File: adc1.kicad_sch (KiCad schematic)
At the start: 57 parts, among them SW1 DRV5055A4QDBZR, SW10 DRV5055A4QDBZR, SW11 DRV5055A4QDBZR, SW12 DRV5055A4QDBZR, SW13 DRV5055A4QDBZR, SW14 DRV5055A4QDBZR, SW15 DRV5055A4QDBZR, SW16 DRV5055A4QDBZR, SW2 DRV5055A4QDBZR, SW3 DRV5055A4QDBZR, SW4 DRV5055A4QDBZR, SW5 DRV5055A4QDBZR, SW6 DRV5055A4QDBZR, SW7 DRV5055A4QDBZR, SW8 DRV5055A4QDBZR, SW9 DRV5055A4QDBZR, U2 ADS7953QDBTRQ1

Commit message: rename untitle.kicad_sch to adc1.kicad_sch
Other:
- title: (none) -> MUX 1
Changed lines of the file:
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@@
 	(generator_version "10.0")
 	(paper "A4")
+	(title_block
+		(title "MUX 1")
+	)
 	(junction
 		(at 149.86 110.49)

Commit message: hierarchical module
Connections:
- net CS1 renamed ~{CS}
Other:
- title: MUX 1 -> ADC 1
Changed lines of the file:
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@@
 	(paper "A4")
 	(title_block
-		(title "MUX 1")
+		(title "ADC 1")
 	)
 	(junction
@@
 		)
 	)
-	(global_label "CS1"
+	(global_label "~{CS}"
 		(shape input)
 		(at 132.08 120.65 0)
@@
 		)
 		(property "Intersheetrefs" "${INTERSHEET_REFS}"
-			(at 138.7542 120.65 0)
+			(at 137.5447 120.65 0)
 			(hide yes)
 			(show_name no)
@@
 		)
 	)
-	(global_label "MISO"
+	(hierarchical_label "MISO"
 		(shape output)
 		(at 132.08 113.03 0)
-		(fields_autoplaced yes)
 		(effects
 			(font
@@
 			(justify left)
 		)
-		(property "Intersheetrefs" "${INTERSHEET_REFS}"
-			(at 139.6614 113.03 0)
-			(hide yes)
-			(show_name no)
-			(do_not_autoplace no)
-			(effects
-				(font
-					(size 1.27 1.27)
-				)
-				(justify left)
-			)
-		)
 	)
 	(symbol
@@
 		(instances
 			(project "stav-keeb-65"
-				(path "/f067c205-942c-45af-b694-038ca43c147c"
-					(reference "#PWR02")
-					(unit 1)
-				)
 				(path "/f067c205-942c-45af-b694-038ca43c147c/7ed9120e-f11c-4b22-935f-1ee89d31afd6"
 					(reference "#PWR02")
@@
 		(instances
 			(project "stav-keeb-65"
-				(path "/f067c205-942c-45af-b694-038ca43c147c"
-					(reference "U2")
-					(unit 1)
-				)
 				(path "/f067c205-942c-45af-b694-038ca43c147c/7ed9120e-f11c-4b22-935f-1ee89d31afd6"
 					(reference "U2")
@@
 		(instances
 			(project "stav-keeb-65"
-				(path "/f067c205-942c-45af-b694-038ca43c147c"
-					(reference "R1")
-					(unit 1)
-				)
 				(path "/f067c205-942c-45af-b694-038ca43c147c/7ed9120e-f11c-4b22-935f-1ee89d31afd6"
 					(reference "R1")
@@
 		(instances
 			(project "stav-keeb-65"
-				(path "/f067c205-942c-45af-b694-038ca43c147c"
-					(reference "SW1")
-					(unit 1)
-				)
 				(path "/f067c205-942c-45af-b694-038ca43c147c/7ed9120e-f11c-4b22-935f-1ee89d31afd6"
 					(reference "SW1")
@@
 		(instances
 			(project "stav-keeb-65"
-				(path "/f067c205-942c-45af-b694-038ca43c147c"
-					(reference "C1")
-					(unit 1)
-				)
 				(path "/f067c205-942c-45af-b694-038ca43c147c/7ed9120e-f11c-4b22-935f-1ee89d31afd6"
 					(reference "C1")

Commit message: Power & USB
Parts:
- C1, C10, C11, C12, C13, C14, C15, C16, C17, C2, C20, C21, C3, C4, C5, C6, C7, C8, C9: footprint Capacitor_SMD:C_0201_0603Metric_Pad0.64x0.40mm_HandSolder -> Capacitor_SMD:C_0603_1608Metric_Pad1.08x0.95mm_HandSolder
- R1, R10, R11, R12, R13, R14, R15, R16, R2, R3, R4, R5, R6, R7, R8, R9: footprint Resistor_SMD:R_0201_0603Metric_Pad0.64x0.40mm_HandSolder -> Resistor_SMD:R_0603_1608Metric_Pad0.98x0.95mm_HandSolder
- R17, R18, R19, R20: footprint Resistor_SMD:R_0201_0603Metric_Pad0.64x0.40mm_HandSolder -> Capacitor_SMD:C_0603_1608Metric_Pad1.08x0.95mm_HandSolder
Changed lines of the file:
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@@
 			)
 		)
-		(property "Footprint" "Capacitor_SMD:C_0201_0603Metric_Pad0.64x0.40mm_HandSolder"
+		(property "Footprint" "Capacitor_SMD:C_0603_1608Metric_Pad1.08x0.95mm_HandSolder"
 			(at 232.41 66.3448 0)
 			(hide yes)
@@
 			)
 		)
-		(property "Footprint" "Resistor_SMD:R_0201_0603Metric_Pad0.64x0.40mm_HandSolder"
+		(property "Footprint" "Resistor_SMD:R_0603_1608Metric_Pad0.98x0.95mm_HandSolder"
 			(at 98.806 131.826 90)
 			(hide yes)
@@
 			)
 		)
-		(property "Footprint" "Capacitor_SMD:C_0201_0603Metric_Pad0.64x0.40mm_HandSolder"
+		(property "Footprint" "Capacitor_SMD:C_0603_1608Metric_Pad1.08x0.95mm_HandSolder"
 			(at 95.25 35.8648 0)
 			(hide yes)
@@
 			)
 		)
-		(property "Footprint" "Capacitor_SMD:C_0201_0603Metric_Pad0.64x0.40mm_HandSolder"
+		(property "Footprint" "Capacitor_SMD:C_0603_1608Metric_Pad1.08x0.95mm_HandSolder"
 			(at 60.96 66.3448 0)
 			(hide yes)
@@
 			)
 		)
-		(property "Footprint" "Capacitor_SMD:C_0201_0603Metric_Pad0.64x0.40mm_HandSolder"
+		(property "Footprint" "Capacitor_SMD:C_0603_1608Metric_Pad1.08x0.95mm_HandSolder"
 			(at 198.12 66.3448 0)
 			(hide yes)
@@
 			)
 		)
-		(property "Footprint" "Capacitor_SMD:C_0201_0603Metric_Pad0.64x0.40mm_HandSolder"
+		(property "Footprint" "Capacitor_SMD:C_0603_1608Metric_Pad1.08x0.95mm_HandSolder"
 			(at 153.3652 125.73 0)
 			(hide yes)
@@
 			)
 		)
-		(property "Footprint" "Resistor_SMD:R_0201_0603Metric_Pad0.64x0.40mm_HandSolder"
+		(property "Footprint" "Resistor_SMD:R_0603_1608Metric_Pad0.98x0.95mm_HandSolder"
 			(at 151.384 134.874 90)
 			(hide yes)
@@
 			)
 		)
-		(property "Footprint" "Capacitor_SMD:C_0201_0603Metric_Pad0.64x0.40mm_HandSolder"
+		(property "Footprint" "Capacitor_SMD:C_0603_1608Metric_Pad1.08x0.95mm_HandSolder"
 			(at 163.83 35.8648 0)
 			(hide yes)
@@
 			)
 		)
-		(property "Footprint" "Resistor_SMD:R_0201_0603Metric_Pad0.64x0.40mm_HandSolder"
+		(property "Footprint" "Capacitor_SMD:C_0603_1608Metric_Pad1.08x0.95mm_HandSolder"
 			(at 132.334 97.536 90)
 			(hide yes)
@@
 			)
 		)
-		(property "Footprint" "Capacitor_SMD:C_0201_0603Metric_Pad0.64x0.40mm_HandSolder"
+		(property "Footprint" "Capacitor_SMD:C_0603_1608Metric_Pad1.08x0.95mm_HandSolder"
 			(at 163.83 66.3448 0)
 			(hide yes)
@@
 			)
 		)
-		(property "Footprint" "Resistor_SMD:R_0201_0603Metric_Pad0.64x0.40mm_HandSolder"
+		(property "Footprint" "Resistor_SMD:R_0603_1608Metric_Pad0.98x0.95mm_HandSolder"
 			(at 151.384 129.794 90)
 			(hide yes)
@@
 			)
 		)
-		(property "Footprint" "Capacitor_SMD:C_0201_0603Metric_Pad0.64x0.40mm_HandSolder"
+		(property "Footprint" "Capacitor_SMD:C_0603_1608Metric_Pad1.08x0.95mm_HandSolder"
 			(at 232.41 35.8648 0)
 			(hide yes)
@@
 			)
 		)
-		(property "Footprint" "Capacitor_SMD:C_0201_0603Metric_Pad0.64x0.40mm_HandSolder"
+		(property "Footprint" "Capacitor_SMD:C_0603_1608Metric_Pad1.08x0.95mm_HandSolder"
 			(at 86.0552 120.65 0)
 			(hide yes)
@@
 			)
 		)
-		(property "Footprint" "Capacitor_SMD:C_0201_0603Metric_Pad0.64x0.40mm_HandSolder"
+		(property "Footprint" "Capacitor_SMD:C_0603_1608Metric_Pad1.08x0.95mm_HandSolder"
 			(at 60.96 35.8648 0)
 			(hide yes)
@@
 			)
 		)
-		(property "Footprint" "Capacitor_SMD:C_0201_0603Metric_Pad0.64x0.40mm_HandSolder"
+		(property "Footprint" "Capacitor_SMD:C_0603_1608Metric_Pad1.08x0.95mm_HandSolder"
 			(at 129.54 35.8648 0)
 			(hide yes)
@@
 			)
 		)
-		(property "Footprint" "Capacitor_SMD:C_0201_0603Metric_Pad0.64x0.40mm_HandSolder"
+		(property "Footprint" "Capacitor_SMD:C_0603_1608Metric_Pad1.08x0.95mm_HandSolder"
 			(at 95.25 66.3448 0)
 			(hide yes)
@@
 			)
 		)
-		(property "Footprint" "Capacitor_SMD:C_0201_0603Metric_Pad0.64x0.40mm_HandSolder"
+		(property "Footprint" "Capacitor_SMD:C_0603_1608Metric_Pad1.08x0.95mm_HandSolder"
 			(at 129.54 66.3447 0)
 			(hide yes)
@@
 			)
 		)
-		(property "Footprint" "Resistor_SMD:R_0201_0603Metric_Pad0.64x0.40mm_HandSolder"
+		(property "Footprint" "Resistor_SMD:R_0603_1608Metric_Pad0.98x0.95mm_HandSolder"
 			(at 134.874 127.254 90)
 			(hide yes)
@@
 			)
 		)
-		(property "Footprint" "Resistor_SMD:R_0201_0603Metric_Pad0.64x0.40mm_HandSolder"
+		(property "Footprint" "Capacitor_SMD:C_0603_1608Metric_Pad1.08x0.95mm_HandSolder"
 			(at 101.854 97.536 90)
 			(hide yes)
@@
 			)
 		)
-		(property "Footprint" "Resistor_SMD:R_0201_0603Metric_Pad0.64x0.40mm_HandSolder"
+		(property "Footprint" "Capacitor_SMD:C_0603_1608Metric_Pad1.08x0.95mm_HandSolder"
 			(at 138.684 97.536 90)
 			(hide yes)
@@
 			)
 		)
-		(property "Footprint" "Capacitor_SMD:C_0201_0603Metric_Pad0.64x0.40mm_HandSolder"
+		(property "Footprint" "Capacitor_SMD:C_0603_1608Metric_Pad1.08x0.95mm_HandSolder"
 			(at 26.67 66.3448 0)
 			(hide yes)
@@
 			)
 		)
-		(property "Footprint" "Capacitor_SMD:C_0201_0603Metric_Pad0.64x0.40mm_HandSolder"
+		(property "Footprint" "Capacitor_SMD:C_0603_1608Metric_Pad1.08x0.95mm_HandSolder"
 			(at 150.8252 110.49 0)
 			(hide yes)
@@
 			)
 		)
-		(property "Footprint" "Resistor_SMD:R_0201_0603Metric_Pad0.64x0.40mm_HandSolder"
+		(property "Footprint" "Resistor_SMD:R_0603_1608Metric_Pad0.98x0.95mm_HandSolder"
 			(at 134.874 132.334 90)
 			(hide yes)
@@
 			)
 		)
-		(property "Footprint" "Resistor_SMD:R_0201_0603Metric_Pad0.64x0.40mm_HandSolder"
+		(property "Footprint" "Resistor_SMD:R_0603_1608Metric_Pad0.98x0.95mm_HandSolder"
 			(at 98.806 136.906 90)
 			(hide yes)
@@
 			)
 		)
-		(property "Footprint" "Resistor_SMD:R_0201_0603Metric_Pad0.64x0.40mm_HandSolder"
+		(property "Footprint" "Capacitor_SMD:C_0603_1608Metric_Pad1.08x0.95mm_HandSolder"
 			(at 95.504 97.536 90)
 			(hide yes)
@@
 			)
 		)
-		(property "Footprint" "Capacitor_SMD:C_0201_0603Metric_Pad0.64x0.40mm_HandSolder"
+		(property "Footprint" "Capacitor_SMD:C_0603_1608Metric_Pad1.08x0.95mm_HandSolder"
 			(at 198.12 35.8648 0)
 			(hide yes)
@@
 			)
 		)
-		(property "Footprint" "Resistor_SMD:R_0201_0603Metric_Pad0.64x0.40mm_HandSolder"
+		(property "Footprint" "Resistor_SMD:R_0603_1608Metric_Pad0.98x0.95mm_HandSolder"
 			(at 98.806 147.066 90)
 			(hide yes)
@@
 			)
 		)
-		(property "Footprint" "Resistor_SMD:R_0201_0603Metric_Pad0.64x0.40mm_HandSolder"
+		(property "Footprint" "Resistor_SMD:R_0603_1608Metric_Pad0.98x0.95mm_HandSolder"
 			(at 81.026 144.526 90)
 			(hide yes)
@@
 			)
 		)
-		(property "Footprint" "Resistor_SMD:R_0201_0603Metric_Pad0.64x0.40mm_HandSolder"
+		(property "Footprint" "Resistor_SMD:R_0603_1608Metric_Pad0.98x0.95mm_HandSolder"
 			(at 81.026 139.446 90)
 			(hide yes)
@@
 			)
 		)
-		(property "Footprint" "Capacitor_SMD:C_0201_0603Metric_Pad0.64x0.40mm_HandSolder"
+		(property "Footprint" "Capacitor_SMD:C_0603_1608Metric_Pad1.08x0.95mm_HandSolder"
 			(at 266.7 35.8647 0)
 			(hide yes)
@@
 			)
 		)
-		(property "Footprint" "Resistor_SMD:R_0201_0603Metric_Pad0.64x0.40mm_HandSolder"
+		(property "Footprint" "Resistor_SMD:R_0603_1608Metric_Pad0.98x0.95mm_HandSolder"
 			(at 81.026 129.286 90)
 			(hide yes)
@@
 			)
 		)
-		(property "Footprint" "Resistor_SMD:R_0201_0603Metric_Pad0.64x0.40mm_HandSolder"
+		(property "Footprint" "Resistor_SMD:R_0603_1608Metric_Pad0.98x0.95mm_HandSolder"
 			(at 134.874 137.414 90)
 			(hide yes)
@@
 			)
 		)
-		(property "Footprint" "Capacitor_SMD:C_0201_0603Metric_Pad0.64x0.40mm_HandSolder"
+		(property "Footprint" "Capacitor_SMD:C_0603_1608Metric_Pad1.08x0.95mm_HandSolder"
 			(at 27.94 35.8648 0)
 			(hide yes)
@@
 			)
 		)
-		(property "Footprint" "Resistor_SMD:R_0201_0603Metric_Pad0.64x0.40mm_HandSolder"
+		(property "Footprint" "Resistor_SMD:R_0603_1608Metric_Pad0.98x0.95mm_HandSolder"
 			(at 151.384 139.954 90)
 			(hide yes)
@@
 			)
 		)
-		(property "Footprint" "Resistor_SMD:R_0201_0603Metric_Pad0.64x0.40mm_HandSolder"
+		(property "Footprint" "Resistor_SMD:R_0603_1608Metric_Pad0.98x0.95mm_HandSolder"
 			(at 81.026 134.366 90)
 			(hide yes)
@@
 			)
 		)
-		(property "Footprint" "Resistor_SMD:R_0201_0603Metric_Pad0.64x0.40mm_HandSolder"
+		(property "Footprint" "Resistor_SMD:R_0603_1608Metric_Pad0.98x0.95mm_HandSolder"
 			(at 134.874 142.494 90)
 			(hide yes)
@@
 			)
 		)
-		(property "Footprint" "Resistor_SMD:R_0201_0603Metric_Pad0.64x0.40mm_HandSolder"
+		(property "Footprint" "Resistor_SMD:R_0603_1608Metric_Pad0.98x0.95mm_HandSolder"
 			(at 98.806 141.986 90)
 			(hide yes)
@@
 			)
 		)
-		(property "Footprint" "Resistor_SMD:R_0201_0603Metric_Pad0.64x0.40mm_HandSolder"
+		(property "Footprint" "Resistor_SMD:R_0603_1608Metric_Pad0.98x0.95mm_HandSolder"
 			(at 151.384 145.034 90)
 			(hide yes)
@@
 			)
 		)
-		(property "Footprint" "Capacitor_SMD:C_0201_0603Metric_Pad0.64x0.40mm_HandSolder"
+		(property "Footprint" "Capacitor_SMD:C_0603_1608Metric_Pad1.08x0.95mm_HandSolder"
 			(at 266.7 66.3447 0)
 			(hide yes)

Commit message: 2.5V ref
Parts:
- added C130: 1uF, Capacitor_SMD:C_0603_1608Metric_Pad1.08x0.95mm_HandSolder, symbol Device:C
- C19: value 10uF -> 100nF; footprint Capacitor_SMD:C_0805_2012Metric_Pad1.18x1.45mm_HandSolder -> Capacitor_SMD:C_0603_1608Metric_Pad1.08x0.95mm_HandSolder; LCSC Part C15850 -> C14663
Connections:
- net GND: now also C19.2, C130.1; no longer C19.1
- net +2V5 renamed +2V5_RREF
- net +2V5_RREF: now also C19.1, C130.2; no longer C19.2

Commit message: Change 2.5V ref to voltage divider
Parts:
- R17, R18, R19, R20: footprint Capacitor_SMD:C_0603_1608Metric_Pad1.08x0.95mm_HandSolder -> Resistor_SMD:R_0603_1608Metric_Pad0.98x0.95mm_HandSolder
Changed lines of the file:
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@@
 			)
 		)
-		(property "Footprint" "Capacitor_SMD:C_0603_1608Metric_Pad1.08x0.95mm_HandSolder"
+		(property "Footprint" "Resistor_SMD:R_0603_1608Metric_Pad0.98x0.95mm_HandSolder"
 			(at 132.334 97.536 90)
 			(hide yes)
@@
 			)
 		)
-		(property "Footprint" "Capacitor_SMD:C_0603_1608Metric_Pad1.08x0.95mm_HandSolder"
+		(property "Footprint" "Resistor_SMD:R_0603_1608Metric_Pad0.98x0.95mm_HandSolder"
 			(at 101.854 97.536 90)
 			(hide yes)
@@
 			)
 		)
-		(property "Footprint" "Capacitor_SMD:C_0603_1608Metric_Pad1.08x0.95mm_HandSolder"
+		(property "Footprint" "Resistor_SMD:R_0603_1608Metric_Pad0.98x0.95mm_HandSolder"
 			(at 138.684 97.536 90)
 			(hide yes)
@@
 			)
 		)
-		(property "Footprint" "Capacitor_SMD:C_0603_1608Metric_Pad1.08x0.95mm_HandSolder"
+		(property "Footprint" "Resistor_SMD:R_0603_1608Metric_Pad0.98x0.95mm_HandSolder"
 			(at 95.504 97.536 90)
 			(hide yes)

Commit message: Review fixes
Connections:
- net +2V5_RREF renamed +2V5_REF

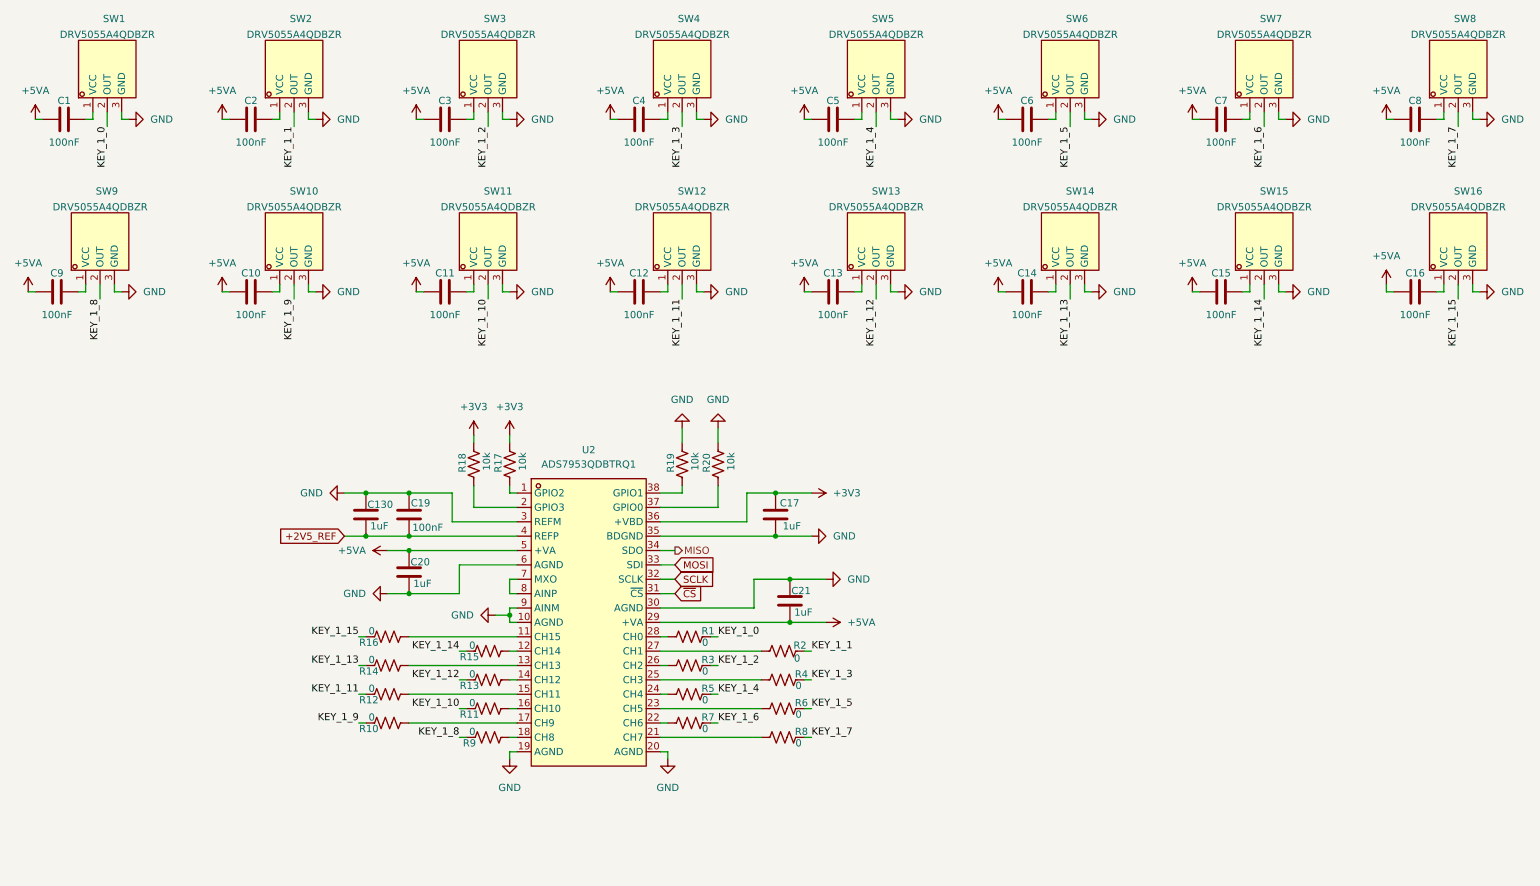
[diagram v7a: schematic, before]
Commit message: initial script for sensor placement, and schematic fixes
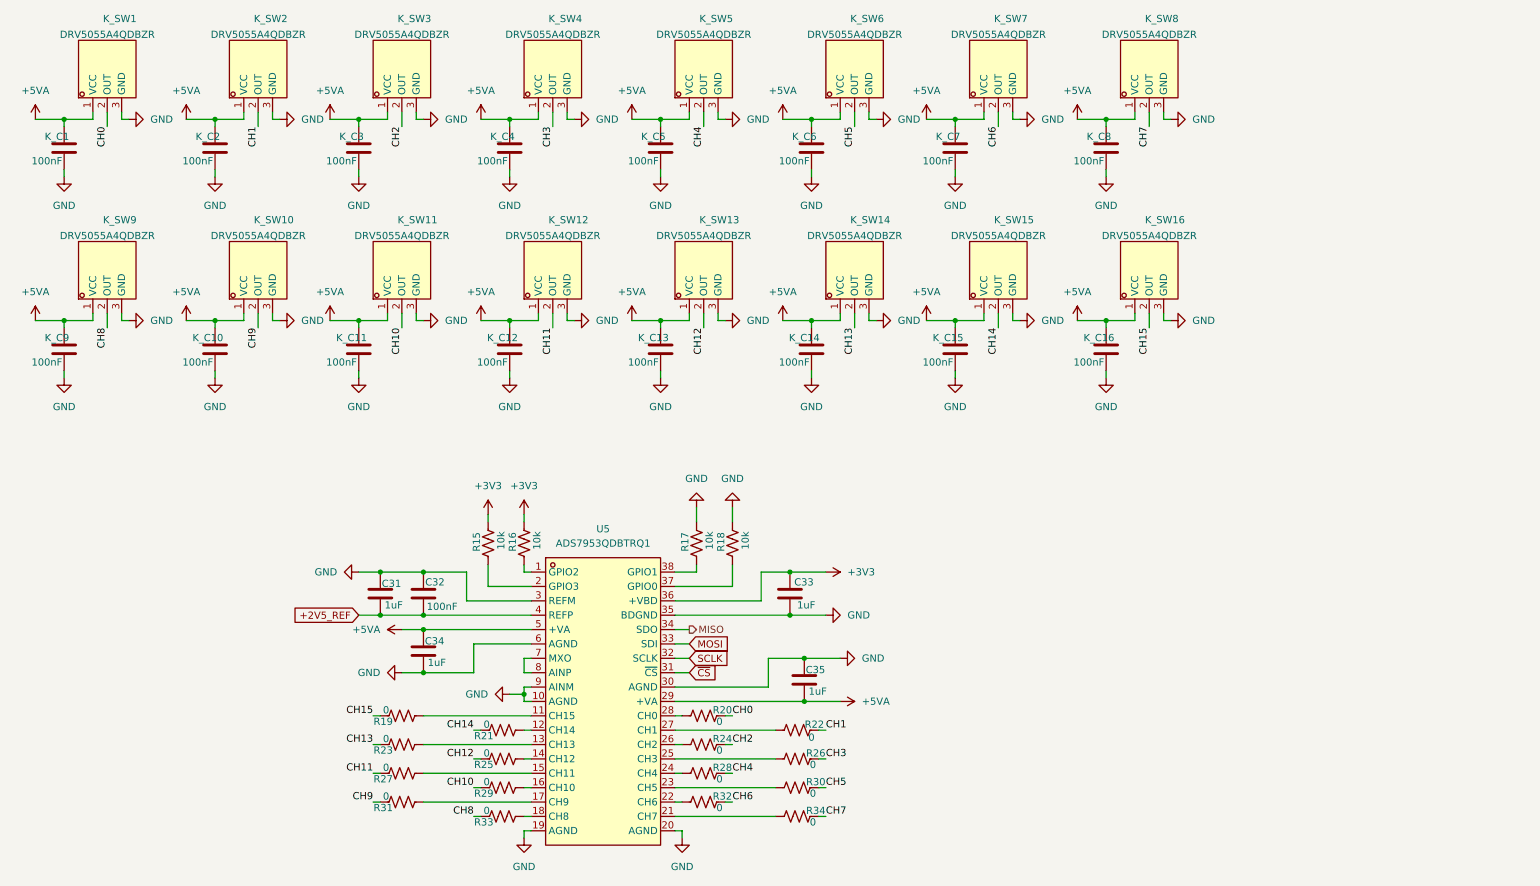
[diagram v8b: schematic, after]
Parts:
- removed C1, C10, C11, C12, C13, C14, C15, C16, C2, C3, C4, C5, C6, C7, C8, C9: 100nF, Capacitor_SMD:C_0603_1608Metric_Pad1.08x0.95mm_HandSolder, symbol Device:C
- removed SW10, SW11, SW12, SW13, SW14, SW15, SW16, SW2, SW3, SW4, SW5, SW6, SW7, SW8, SW9: DRV5055A4QDBZR, easyeda2kicad:SOT-23-3_L2.9-W1.3-P1.90-LS2.4-BR, symbol easyeda2kicad:DRV5055A4QDBZR
- added K_C1, K_C10, K_C11, K_C12, K_C13, K_C14, K_C15, K_C16, K_C2, K_C3, K_C4, K_C5, K_C6, K_C7, K_C8, K_C9: 100nF, Capacitor_SMD:C_0603_1608Metric_Pad1.08x0.95mm_HandSolder, symbol Device:C
- added K_SW10, K_SW11, K_SW12, K_SW13, K_SW14, K_SW15, K_SW16, K_SW2, K_SW3, K_SW4, K_SW5, K_SW6, K_SW7, K_SW8, K_SW9: DRV5055A4QDBZR, easyeda2kicad:SOT-23-3_L2.9-W1.3-P1.90-LS2.4-BR, symbol easyeda2kicad:DRV5055A4QDBZR
- renumbered C130 to C31, C19 to C32, C17 to C33, C20 to C34, C21 to C35, SW1 to K_SW1, R18 to R15, R17 to R16, R19 to R17, R20 to R18, R16 to R19, R1 to R20, R15 to R21, R2 to R22, R14 to R23, R3 to R24, R13 to R25, R4 to R26, R12 to R27, R5 to R28, R11 to R29, R6 to R30, R10 to R31, R7 to R32, R9 to R33, R8 to R34, U2 to U5
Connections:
- net +5VA: now also K_SW1.1 (VCC), K_C1.2, K_C10.2, K_C11.2, K_C12.2, K_C13.2, K_C14.2, K_C15.2, K_C16.2, K_C2.2, K_C3.2, K_C4.2, K_C5.2, K_C6.2, K_C7.2, K_C8.2, K_C9.2, K_SW10.1 (VCC), K_SW11.1 (VCC), K_SW12.1 (VCC), K_SW13.1 (VCC), K_SW14.1 (VCC), K_SW15.1 (VCC), K_SW16.1 (VCC), K_SW2.1 (VCC), K_SW3.1 (VCC), K_SW4.1 (VCC), K_SW5.1 (VCC), K_SW6.1 (VCC), K_SW7.1 (VCC), K_SW8.1 (VCC), K_SW9.1 (VCC)
- net GND: now also K_C1.1, K_C10.1, K_C11.1, K_C12.1, K_C13.1, K_C14.1, K_C15.1, K_C16.1, K_C2.1, K_C3.1, K_C4.1, K_C5.1, K_C6.1, K_C7.1, K_C8.1, K_C9.1, K_SW10.3 (GND), K_SW11.3 (GND), K_SW12.3 (GND), K_SW13.3 (GND), K_SW14.3 (GND), K_SW15.3 (GND), K_SW16.3 (GND), K_SW2.3 (GND), K_SW3.3 (GND), K_SW4.3 (GND), K_SW5.3 (GND), K_SW6.3 (GND), K_SW7.3 (GND), K_SW8.3 (GND), K_SW9.3 (GND)
- net KEY_1_0 renamed CH0
- net KEY_1_1 renamed CH1
- net CH1: now also K_SW2.2 (OUT)
- net KEY_1_10 renamed CH10
- net CH10: now also K_SW11.2 (OUT)
- net KEY_1_11 renamed CH11
- net CH11: now also K_SW12.2 (OUT)
- net KEY_1_12 renamed CH12
- net CH12: now also K_SW13.2 (OUT)
- net KEY_1_13 renamed CH13
- net CH13: now also K_SW14.2 (OUT)
- net KEY_1_14 renamed CH14
- net CH14: now also K_SW15.2 (OUT)
- net KEY_1_15 renamed CH15
- net CH15: now also K_SW16.2 (OUT)
- net KEY_1_2 renamed CH2
- net CH2: now also K_SW3.2 (OUT)
- net KEY_1_3 renamed CH3
- net CH3: now also K_SW4.2 (OUT)
- net KEY_1_4 renamed CH4
- net CH4: now also K_SW5.2 (OUT)
- net KEY_1_5 renamed CH5
- net CH5: now also K_SW6.2 (OUT)
- net KEY_1_6 renamed CH6
- net CH6: now also K_SW7.2 (OUT)
- net KEY_1_7 renamed CH7
- net CH7: now also K_SW8.2 (OUT)
- net KEY_1_8 renamed CH8
- net CH8: now also K_SW9.2 (OUT)
- net KEY_1_9 renamed CH9
- net CH9: now also K_SW10.2 (OUT)
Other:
- moved on the sheet: C31, C32, C33, C34, C35, R15, R16, R17, R18, R19, R20, R21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
